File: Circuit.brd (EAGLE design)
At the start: 82.4 x 109.5 mm, 8 parts

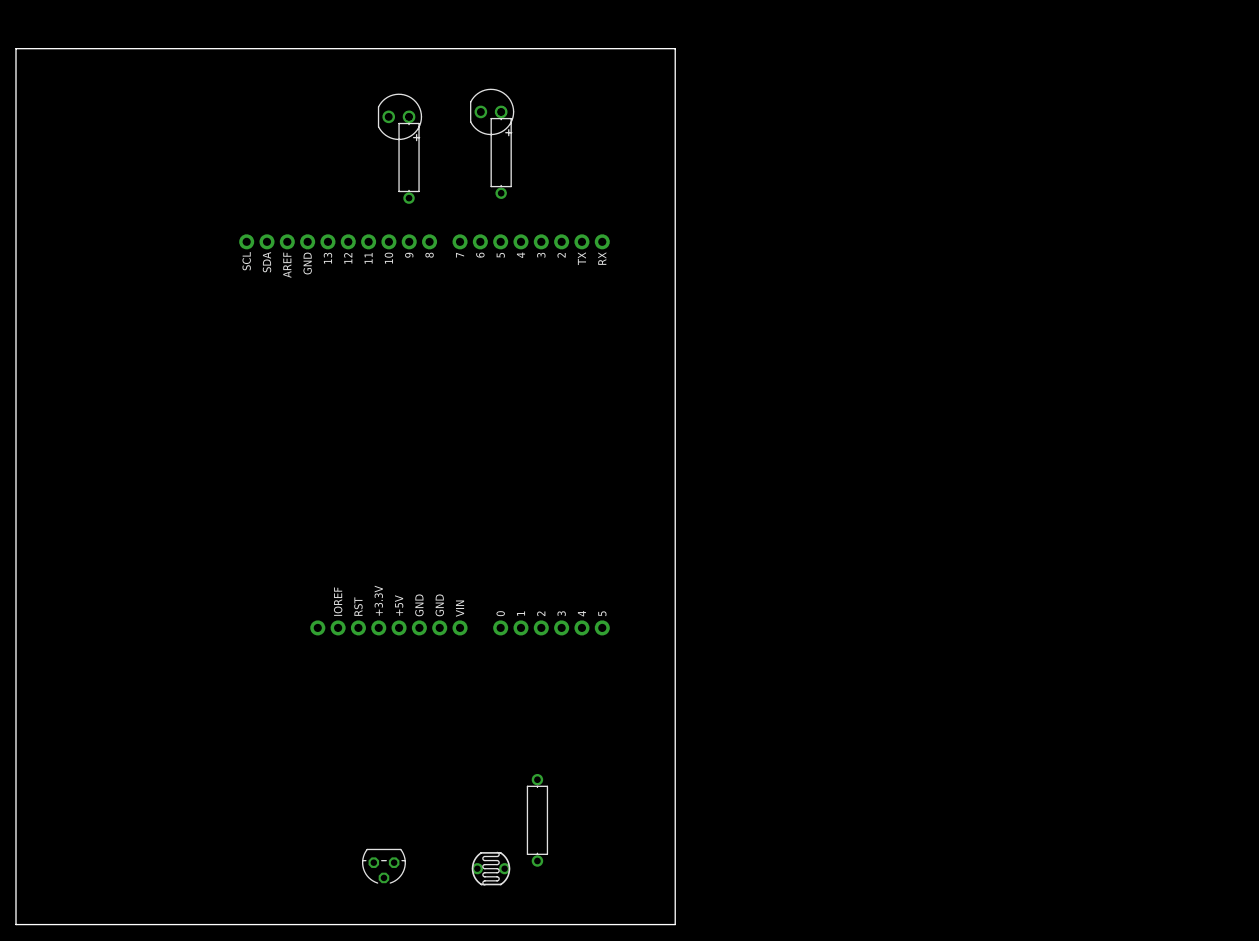
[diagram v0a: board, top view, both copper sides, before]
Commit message: added: LCD screen
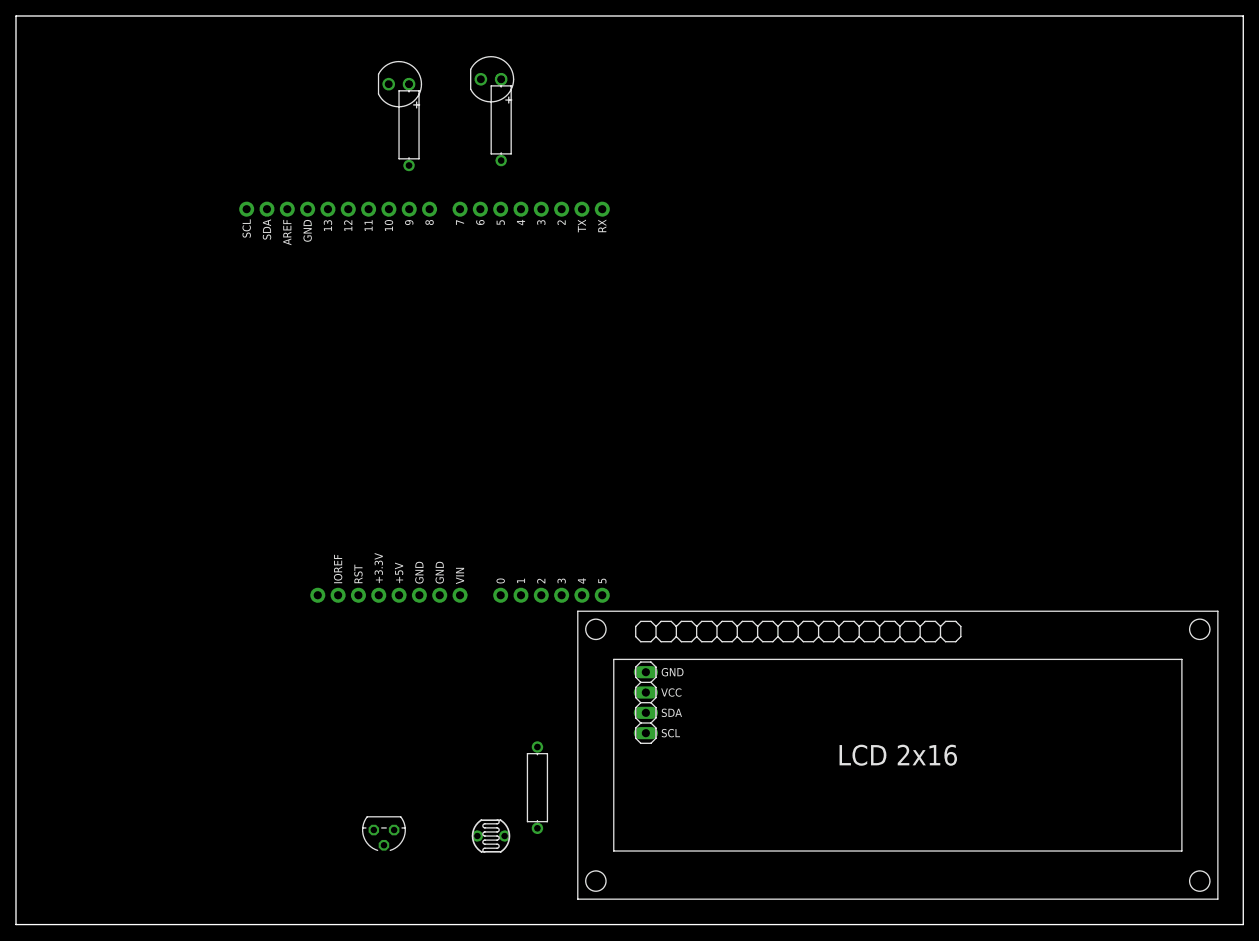
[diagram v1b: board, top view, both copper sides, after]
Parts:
- added U1: LCD-16X2-I2CSUNFOUNDER-IIC, Tinkercad:LCD-I2C
- moved DFAN 4.08 mm to (59.4, 105.7)
- moved DLIGHT 4.08 mm to (47.9, 105.0)
- moved R4 4.08 mm to (60.6, 100.6)
- moved RRESISTOR 4.08 mm to (65.2, 17.1)
- moved UMAIN_BOARD 4.08 mm to (47.9, 65.3)
- moved R1 4.08 mm to (59.4, 11.1)
- moved UTEMPERATURE_SENSOR 4.08 mm to (46.0, 11.8)
- moved R3 4.08 mm to (49.1, 100.0)
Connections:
- new net UMAIN_BOARD_A4: U1.3, UMAIN_BOARD.A4
- new net UMAIN_BOARD_A5: U1.4, UMAIN_BOARD.A5
- net UMAIN_BOARD_5V: now also U1.2
- net UMAIN_BOARD_GND: now also U1.1
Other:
- board size 82.4 x 109.5 mm -> 153.4 x 113.6 mm
